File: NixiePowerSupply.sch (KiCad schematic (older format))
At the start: 17 parts, among them J1 BARREL_JACK, P1 CONN_01X03, P2 CONN_01X03, T1 IRF644, U1 MAX1771

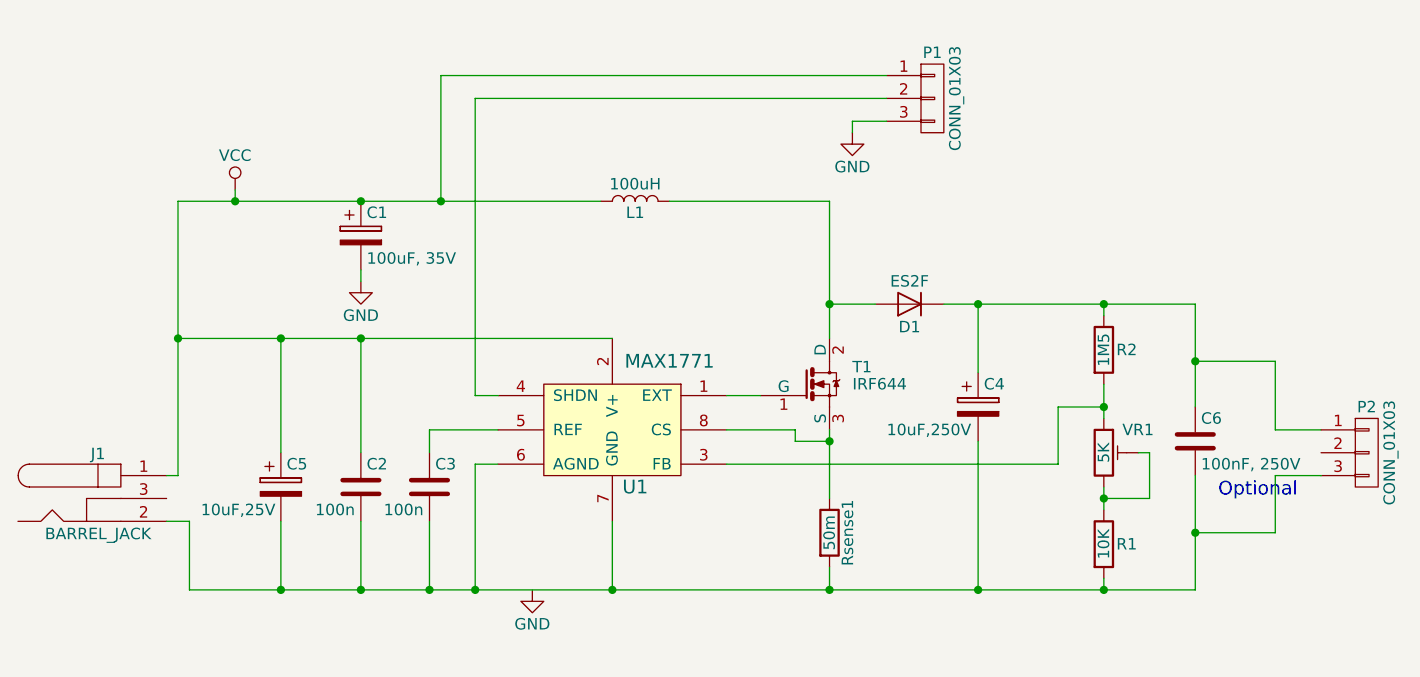
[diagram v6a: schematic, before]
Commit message: Added some tracks.
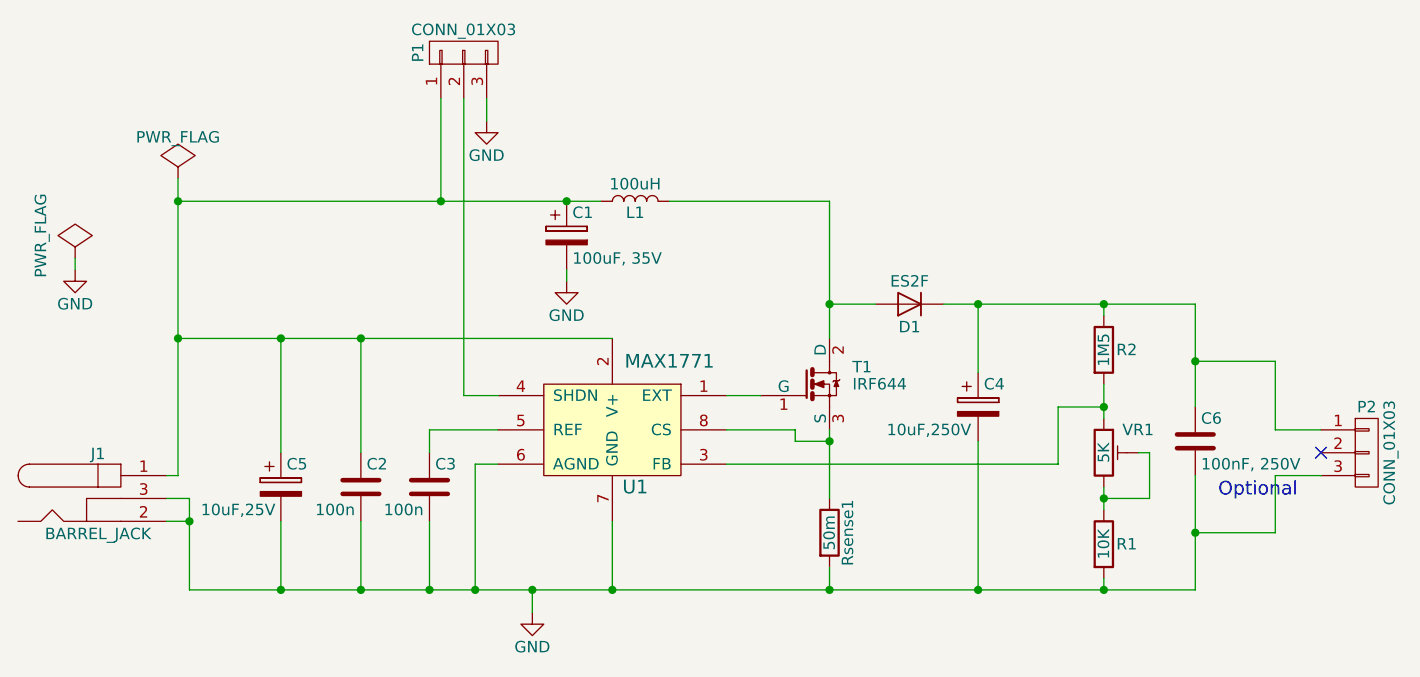
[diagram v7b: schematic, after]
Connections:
- net GND: now also C2.2, C3.2, C4.2, C5.2, C6.2, J1.2, J1.3, P2.3 (P3), R1.2, Rsense1.2, U1.6 (AGND), U1.7 (GND)
- net VCC: no longer names the net of C1.1, C2.1, C5.1, J1.1, L1.1, P1.1 (P1), U1.2 (V+)
- no-connect marks 0 -> 1
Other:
- moved on the sheet: C1, P1
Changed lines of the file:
@@
 L CP C1
 U 1 1 58D7257E
-P 4650 2750
-F 0 "C1" H 4675 2850 50  0000 L CNN
-F 1 "100uF, 35V" H 4675 2650 50  0000 L CNN
-F 2 "Capacitors_Tantalum_SMD:CP_Tantalum_Case-X_EIA-7343-43_Hand" H 4688 2600 50  0001 C CNN
-F 3 "" H 4650 2750 50  0001 C CNN
-	1    4650 2750
+P 5550 2750
+F 0 "C1" H 5575 2850 50  0000 L CNN
+F 1 "100uF, 35V" H 5575 2650 50  0000 L CNN
+F 2 "Capacitors_Tantalum_SMD:CP_Tantalum_Case-X_EIA-7343-43_Hand" H 5588 2600 50  0001 C CNN
+F 3 "" H 5550 2750 50  0001 C CNN
+	1    5550 2750
 	1    0    0    -1
 $EndComp
@@
 L GND #PWR01
 U 1 1 58D72A4A
-P 4650 2950
-F 0 "#PWR01" H 4650 2700 50  0001 C CNN
-F 1 "GND" H 4650 2800 50  0000 C CNN
-F 2 "" H 4650 2950 50  0001 C CNN
-F 3 "" H 4650 2950 50  0001 C CNN
-	1    4650 2950
-	1    0    0    -1
-$EndComp
-Wire Wire Line
-	3850 2600 5700 2600
-Connection ~ 4650 2600
-Wire Wire Line
-	6700 2600 6700 3200
+P 5550 2950
+F 0 "#PWR01" H 5550 2700 50  0001 C CNN
+F 1 "GND" H 5550 2800 50  0000 C CNN
+F 2 "" H 5550 2950 50  0001 C CNN
+F 3 "" H 5550 2950 50  0001 C CNN
+	1    5550 2950
+	1    0    0    -1
+$EndComp
 $Comp
 L CP C5
@@
 	1    0    0    -1
 $EndComp
-Wire Wire Line
-	4650 2900 4650 2950
-$Comp
-L VCC #PWR02
-U 1 1 58D72D8A
-P 4100 2550
-F 0 "#PWR02" H 4100 2400 50  0001 C CNN
-F 1 "VCC" H 4100 2700 50  0000 C CNN
-F 2 "" H 4100 2550 50  0001 C CNN
-F 3 "" H 4100 2550 50  0001 C CNN
-	1    4100 2550
-	1    0    0    -1
-$EndComp
-Wire Wire Line
-	3850 3200 5750 3200
 $Comp
 L C C2
@@
 	1    0    0    -1
 $EndComp
-Wire Wire Line
-	5250 3600 4950 3600
-Wire Wire Line
-	4950 3600 4950 3700
-Wire Wire Line
-	4300 3700 4300 3200
-Connection ~ 4300 3200
-Wire Wire Line
-	4650 3700 4650 3200
-Connection ~ 4650 3200
-Wire Wire Line
-	5750 4300 5750 4000
-Wire Wire Line
-	8300 4300 3900 4300
-$Comp
-L GND #PWR03
+$Comp
+L GND #PWR02
 U 1 1 58D73109
-P 5400 4300
-F 0 "#PWR03" H 5400 4050 50  0001 C CNN
-F 1 "GND" H 5400 4150 50  0000 C CNN
-F 2 "" H 5400 4300 50  0001 C CNN
-F 3 "" H 5400 4300 50  0001 C CNN
-	1    5400 4300
+P 5400 4400
+F 0 "#PWR02" H 5400 4150 50  0001 C CNN
+F 1 "GND" H 5400 4250 50  0000 C CNN
+F 2 "" H 5400 4400 50  0001 C CNN
+F 3 "" H 5400 4400 50  0001 C CNN
+	1    5400 4400
 	1    0    0    -1
 $EndComp
@@
 	1    0    0    -1
 $EndComp
-Wire Wire Line
-	3850 2600 3850 3800
-Connection ~ 3850 3200
-Connection ~ 4100 2600
-Wire Wire Line
-	4100 2550 4100 2600
-Wire Wire Line
-	4300 4000 4300 4300
-Connection ~ 4300 4300
-Wire Wire Line
-	4650 4000 4650 4300
-Connection ~ 4650 4300
-Wire Wire Line
-	4950 4000 4950 4300
-Connection ~ 4950 4300
-Wire Wire Line
-	5250 3750 5150 3750
-Wire Wire Line
-	5150 3750 5150 4300
-Connection ~ 5150 4300
 $Comp
 L R Rsense1
@@
 	1    0    0    -1
 $EndComp
-Wire Wire Line
-	6700 4300 6700 4200
-Connection ~ 5750 4300
-Wire Wire Line
-	6700 3600 6700 3900
-Wire Wire Line
-	6550 3600 6550 3650
-Wire Wire Line
-	6550 3650 6700 3650
-Connection ~ 6700 3650
 $Comp
 L D D1
@@
 	1    0    0    -1
 $EndComp
-Wire Wire Line
-	6900 3050 6700 3050
-Connection ~ 6700 3050
-Wire Wire Line
-	7200 3050 8300 3050
-Wire Wire Line
-	7350 3050 7350 3350
-Wire Wire Line
-	7350 4300 7350 3650
-Connection ~ 6700 4300
 $Comp
 L R R2
@@
 	1    0    0    -1
 $EndComp
-Wire Wire Line
-	7900 3850 7900 3950
-Wire Wire Line
-	7900 3050 7900 3100
-Connection ~ 7350 3050
-Wire Wire Line
-	7900 3400 7900 3550
-Wire Wire Line
-	7900 4300 7900 4250
-Connection ~ 7350 4300
-Wire Wire Line
-	7700 3750 7700 3500
-Wire Wire Line
-	7700 3500 7900 3500
-Connection ~ 7900 3500
 $Comp
 L C C6
@@
 	1    0    0    -1
 $EndComp
-Wire Wire Line
-	6000 2600 6700 2600
-Wire Wire Line
-	6250 3450 6400 3450
-Wire Wire Line
-	6250 3600 6550 3600
-Wire Wire Line
-	6250 3750 7700 3750
-Wire Wire Line
-	8300 3050 8300 3500
-Connection ~ 7900 3050
-Wire Wire Line
-	8300 3800 8300 4300
-Connection ~ 7900 4300
-Wire Wire Line
-	8300 3300 8650 3300
-Connection ~ 8300 3300
-Wire Wire Line
-	8300 4050 8650 4050
-Connection ~ 8300 4050
-Wire Wire Line
-	3850 3800 3800 3800
-Wire Wire Line
-	3900 4300 3900 4000
-Wire Wire Line
-	3900 4000 3800 4000
 $Comp
 L POT_TRIM VR1
@@
 	1    0    0    -1
 $EndComp
-Wire Wire Line
-	7900 3900 8100 3900
-Wire Wire Line
-	8100 3900 8100 3700
-Wire Wire Line
-	8100 3700 8050 3700
-Connection ~ 7900 3900
 Text Notes 8400 3900 0    60   ~ 0
 Optional
@@
 	1    0    0    -1
 $EndComp
-Wire Wire Line
-	8650 3300 8650 3600
-Wire Wire Line
-	8650 3600 8850 3600
-Wire Wire Line
-	8650 4050 8650 3800
-Wire Wire Line
-	8650 3800 8850 3800
 $Comp
 L CONN_01X03 P1
 U 1 1 58DB3DD2
-P 7150 2150
-F 0 "P1" H 7150 2350 50  0000 C CNN
-F 1 "CONN_01X03" V 7250 2150 50  0000 C CNN
-F 2 "Pin_Headers:Pin_Header_Straight_1x03_Pitch2.54mm" H 7150 2150 50  0001 C CNN
-F 3 "" H 7150 2150 50  0000 C CNN
-	1    7150 2150
-	1    0    0    -1
-$EndComp
-Wire Wire Line
-	5000 2600 5000 2050
-Wire Wire Line
-	5000 2050 6950 2050
+P 5100 1950
+F 0 "P1" H 5100 2150 50  0000 C CNN
+F 1 "CONN_01X03" V 5200 1950 50  0000 C CNN
+F 2 "Pin_Headers:Pin_Header_Straight_1x03_Pitch2.54mm" H 5100 1950 50  0001 C CNN
+F 3 "" H 5100 1950 50  0000 C CNN
+	1    5100 1950
+	0    -1   -1   0
+$EndComp
+$Comp
+L GND #PWR03
+U 1 1 58DB402E
+P 5200 2250
+F 0 "#PWR03" H 5200 2000 50  0001 C CNN
+F 1 "GND" H 5200 2100 50  0000 C CNN
+F 2 "" H 5200 2250 50  0000 C CNN
+F 3 "" H 5200 2250 50  0000 C CNN
+	1    5200 2250
+	1    0    0    -1
+$EndComp
+NoConn ~ 8850 3700
+$Comp
+L PWR_FLAG #FLG04
+U 1 1 58DDC3D9
+P 3850 2500
+F 0 "#FLG04" H 3850 2595 50  0001 C CNN
+F 1 "PWR_FLAG" H 3850 2680 50  0000 C CNN
+F 2 "" H 3850 2500 50  0000 C CNN
+F 3 "" H 3850 2500 50  0000 C CNN
+	1    3850 2500
+	1    0    0    -1
+$EndComp
+$Comp
+L PWR_FLAG #FLG05
+U 1 1 58DDC889
+P 3400 2850
+F 0 "#FLG05" H 3400 2945 50  0001 C CNN
+F 1 "PWR_FLAG" V 3250 2950 50  0000 C CNN
+F 2 "" H 3400 2850 50  0000 C CNN
+F 3 "" H 3400 2850 50  0000 C CNN
+	1    3400 2850
+	1    0    0    -1
+$EndComp
+$Comp
+L GND #PWR06
+U 1 1 58DDCB98
+P 3400 2900
+F 0 "#PWR06" H 3400 2650 50  0001 C CNN
+F 1 "GND" H 3400 2750 50  0000 C CNN
+F 2 "" H 3400 2900 50  0000 C CNN
+F 3 "" H 3400 2900 50  0000 C CNN
+	1    3400 2900
+	1    0    0    -1
+$EndComp
+Wire Wire Line
+	3400 2900 3400 2850
+Connection ~ 5400 4300
+Wire Wire Line
+	5400 4400 5400 4300
+Connection ~ 3850 2600
+Wire Wire Line
+	5100 2150 5100 3450
+Wire Wire Line
+	5000 2150 5000 2600
+Connection ~ 3900 4000
+Wire Wire Line
+	3800 3900 3900 3900
+Wire Wire Line
+	5200 2250 5200 2150
+Wire Wire Line
+	5100 3450 5250 3450
 Connection ~ 5000 2600
 Wire Wire Line
-	5250 3450 5150 3450
-Wire Wire Line
-	5150 3450 5150 2150
-Wire Wire Line
-	5150 2150 6950 2150
-$Comp
-L GND #PWR04
-U 1 1 58DB402E
-P 6800 2300
-F 0 "#PWR04" H 6800 2050 50  0001 C CNN
-F 1 "GND" H 6800 2150 50  0000 C CNN
-F 2 "" H 6800 2300 50  0000 C CNN
-F 3 "" H 6800 2300 50  0000 C CNN
-	1    6800 2300
-	1    0    0    -1
-$EndComp
-Wire Wire Line
-	6800 2300 6800 2250
-Wire Wire Line
-	6800 2250 6950 2250
+	8650 3800 8850 3800
+Wire Wire Line
+	8650 4050 8650 3800
+Wire Wire Line
+	8650 3600 8850 3600
+Wire Wire Line
+	8650 3300 8650 3600
+Connection ~ 7900 3900
+Wire Wire Line
+	8100 3700 8050 3700
+Wire Wire Line
+	8100 3900 8100 3700
+Wire Wire Line
+	7900 3900 8100 3900
+Wire Wire Line
+	3900 4000 3800 4000
+Wire Wire Line
+	3900 3900 3900 4300
+Wire Wire Line
+	3850 3800 3800 3800
+Connection ~ 8300 4050
+Wire Wire Line
+	8300 4050 8650 4050
+Connection ~ 8300 3300
+Wire Wire Line
+	8300 3300 8650 3300
+Connection ~ 7900 4300
+Wire Wire Line
+	8300 4300 8300 3800
+Connection ~ 7900 3050
+Wire Wire Line
+	8300 3050 8300 3500
+Wire Wire Line
+	6250 3750 7700 3750
+Wire Wire Line
+	6250 3600 6550 3600
+Wire Wire Line
+	6250 3450 6400 3450
+Wire Wire Line
+	6000 2600 6700 2600
+Connection ~ 7900 3500
+Wire Wire Line
+	7700 3500 7900 3500
+Wire Wire Line
+	7700 3750 7700 3500
+Connection ~ 7350 4300
+Wire Wire Line
+	7900 4300 7900 4250
+Wire Wire Line
+	7900 3400 7900 3550
+Connection ~ 7350 3050
+Wire Wire Line
+	7900 3050 7900 3100
+Wire Wire Line
+	7900 3850 7900 3950
+Connection ~ 6700 4300
+Wire Wire Line
+	7350 4300 7350 3650
+Wire Wire Line
+	7350 3050 7350 3350
+Wire Wire Line
+	7200 3050 8300 3050
+Connection ~ 6700 3050
+Wire Wire Line
+	6900 3050 6700 3050
+Connection ~ 6700 3650
+Wire Wire Line
+	6550 3650 6700 3650
+Wire Wire Line
+	6550 3600 6550 3650
+Wire Wire Line
+	6700 3600 6700 3900
+Connection ~ 5750 4300
+Wire Wire Line
+	6700 4300 6700 4200
+Connection ~ 5150 4300
+Wire Wire Line
+	5150 3750 5150 4300
+Wire Wire Line
+	5250 3750 5150 3750
+Connection ~ 4950 4300
+Wire Wire Line
+	4950 4000 4950 4300
+Connection ~ 4650 4300
+Wire Wire Line
+	4650 4000 4650 4300
+Connection ~ 4300 4300
+Wire Wire Line
+	4300 4000 4300 4300
+Connection ~ 3850 3200
+Wire Wire Line
+	3850 2500 3850 3800
+Wire Wire Line
+	5750 4300 5750 4000
+Connection ~ 4650 3200
+Wire Wire Line
+	4650 3700 4650 3200
+Connection ~ 4300 3200
+Wire Wire Line
+	4300 3700 4300 3200
+Wire Wire Line
+	4950 3600 4950 3700
+Wire Wire Line
+	5250 3600 4950 3600
+Wire Wire Line
+	3850 3200 5750 3200
+Wire Wire Line
+	5550 2900 5550 2950
+Wire Wire Line
+	6700 2600 6700 3200
+Connection ~ 5550 2600
+Wire Wire Line
+	3850 2600 5700 2600
+Wire Wire Line
+	3900 4300 8300 4300
 $EndSCHEMATC

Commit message: Fixed output connector
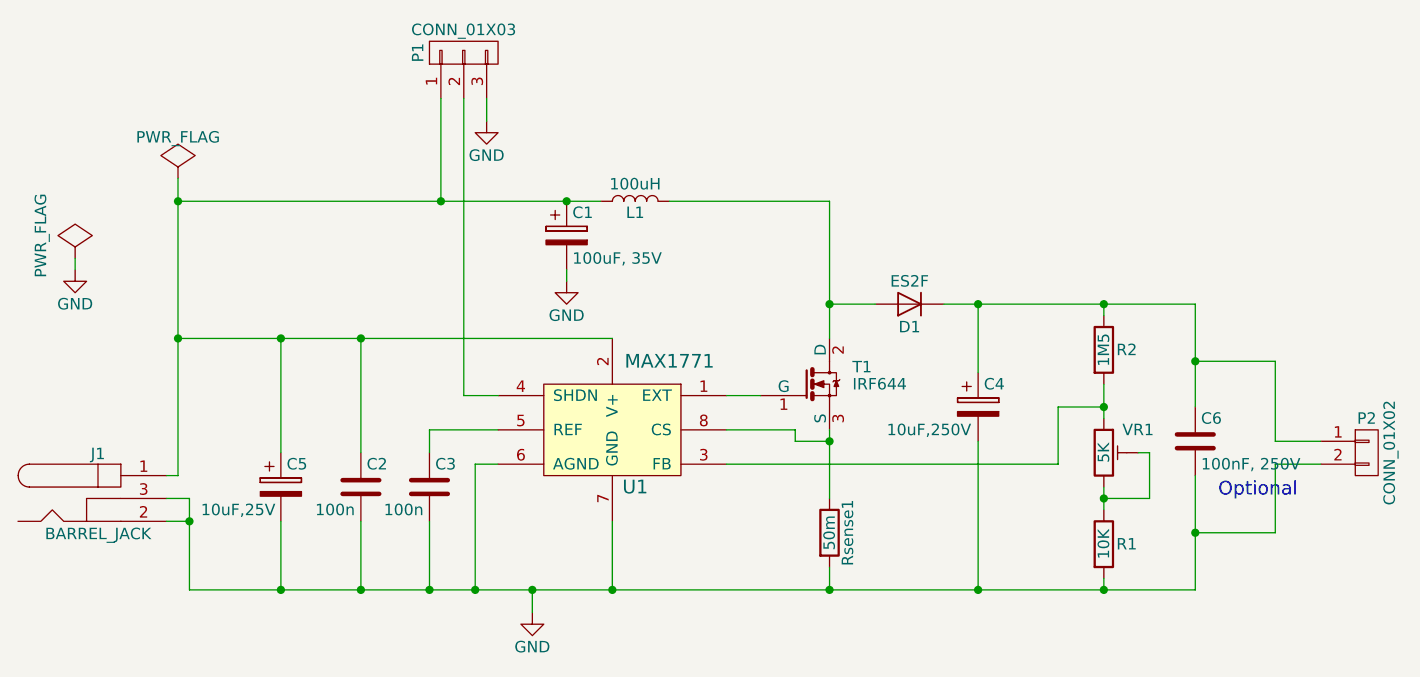
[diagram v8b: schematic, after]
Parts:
- removed P2: CONN_01X03, Pin_Headers:Pin_Header_Straight_1x03_Pitch2.54mm, symbol CONN_01X03
- added P2: CONN_01X02, symbol CONN_01X02
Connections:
- net GND: now also P2.2 (P2)
- net at C4.1, C6.1, D1.1 (K)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: now also P2.1 (P1)
- no-connect marks 1 -> 0
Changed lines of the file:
@@
 Optional
-$Comp
-L CONN_01X03 P2
-U 1 1 58DB3C7B
-P 9050 3700
-F 0 "P2" H 9050 3900 50  0000 C CNN
-F 1 "CONN_01X03" V 9150 3700 50  0000 C CNN
-F 2 "Pin_Headers:Pin_Header_Straight_1x03_Pitch2.54mm" H 9050 3700 50  0001 C CNN
-F 3 "" H 9050 3700 50  0000 C CNN
-	1    9050 3700
-	1    0    0    -1
-$EndComp
 $Comp
 L CONN_01X03 P1
@@
 	1    0    0    -1
 $EndComp
-NoConn ~ 8850 3700
 $Comp
 L PWR_FLAG #FLG04
@@
 Connection ~ 5400 4300
 Wire Wire Line
-	5400 4400 5400 4300
+	5400 4300 5400 4400
 Connection ~ 3850 2600
 Wire Wire Line
@@
 Connection ~ 5000 2600
 Wire Wire Line
-	8650 3800 8850 3800
-Wire Wire Line
-	8650 4050 8650 3800
-Wire Wire Line
-	8650 3600 8850 3600
-Wire Wire Line
-	8650 3300 8650 3600
+	8650 3750 8850 3750
+Wire Wire Line
+	8650 3750 8650 4050
+Wire Wire Line
+	8650 3650 8850 3650
+Wire Wire Line
+	8650 3300 8650 3650
 Connection ~ 7900 3900
 Wire Wire Line
@@
 Connection ~ 8300 4050
 Wire Wire Line
-	8300 4050 8650 4050
+	8650 4050 8300 4050
 Connection ~ 8300 3300
 Wire Wire Line
@@
 Connection ~ 5150 4300
 Wire Wire Line
-	5150 3750 5150 4300
-Wire Wire Line
-	5250 3750 5150 3750
+	5150 4300 5150 3750
+Wire Wire Line
+	5150 3750 5250 3750
 Connection ~ 4950 4300
 Wire Wire Line
-	4950 4000 4950 4300
+	4950 4300 4950 4000
 Connection ~ 4650 4300
 Wire Wire Line
-	4650 4000 4650 4300
+	4650 4300 4650 4000
 Connection ~ 4300 4300
 Wire Wire Line
@@
 Connection ~ 4650 3200
 Wire Wire Line
-	4650 3700 4650 3200
+	4650 3200 4650 3700
 Connection ~ 4300 3200
 Wire Wire Line
@@
 Wire Wire Line
 	3900 4300 8300 4300
+$Comp
+L CONN_01X02 P2
+U 1 1 58EB00E3
+P 9050 3700
+F 0 "P2" H 9050 3850 50  0000 C CNN
+F 1 "CONN_01X02" V 9150 3700 50  0000 C CNN
+F 2 "" H 9050 3700 50  0000 C CNN
+F 3 "" H 9050 3700 50  0000 C CNN
+	1    9050 3700
+	1    0    0    -1
+$EndComp
 $EndSCHEMATC
